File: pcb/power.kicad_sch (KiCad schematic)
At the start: 43 parts, among them Q1 AO3407A, Q2 PMV20EN, Q3 NCE3401AY, Q4 NCE3401AY, Q5 DMMT5401, U2 AP63200T

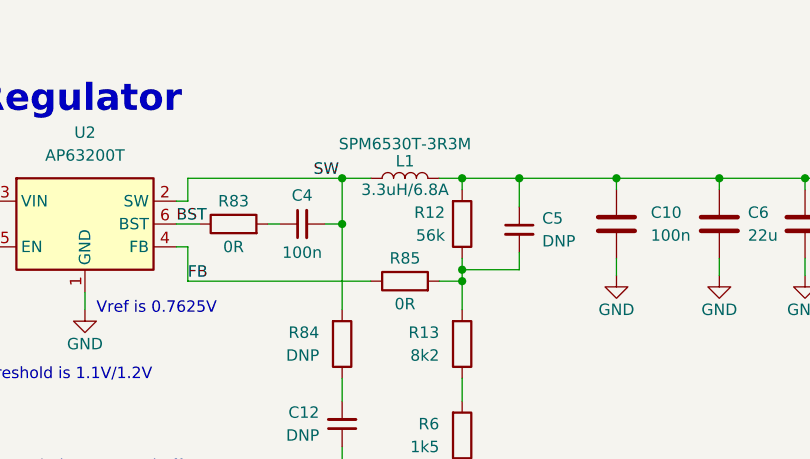
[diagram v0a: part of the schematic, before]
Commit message: Update to kicad 8
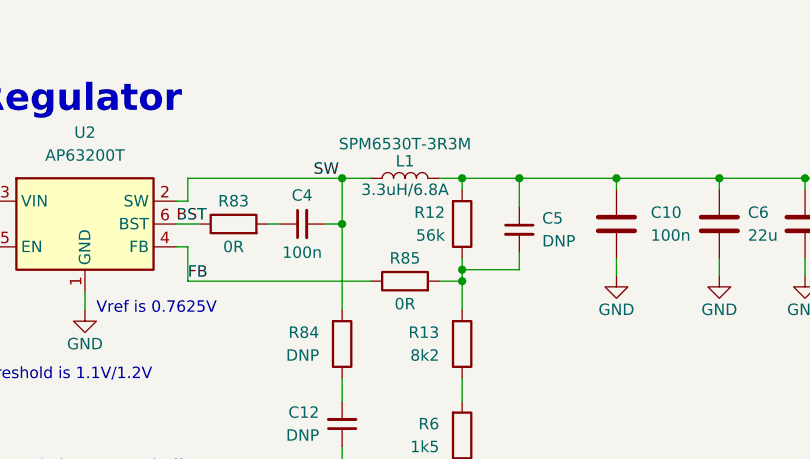
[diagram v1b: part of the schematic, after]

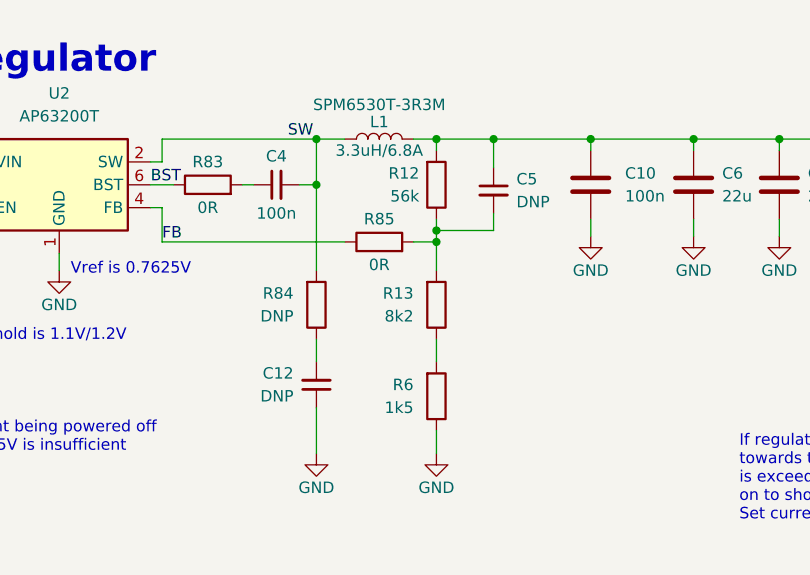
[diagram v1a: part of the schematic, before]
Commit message: Fix JLC part association
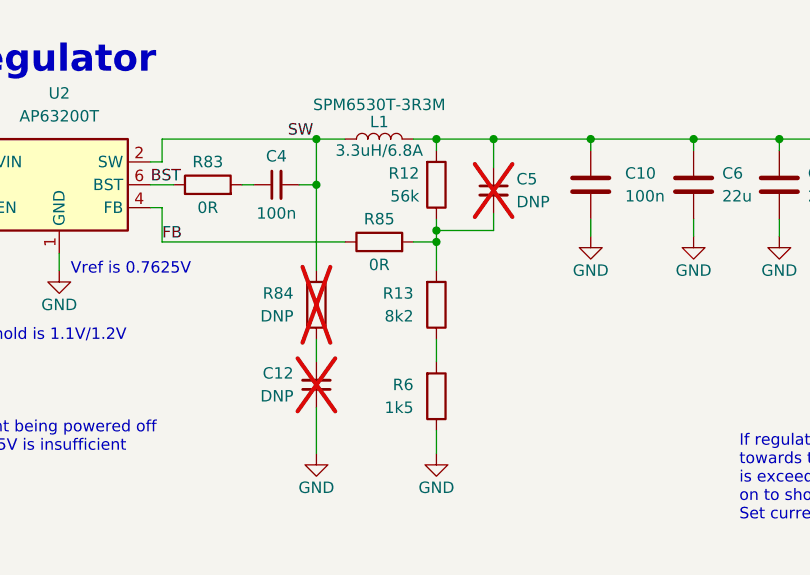
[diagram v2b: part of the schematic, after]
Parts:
- C10, C4, C9: JLC (none) -> C307331
- C11, C3, C6, C7, C8: JLC (none) -> C12891
- C12, C5, R84: now not fitted
- D2: JLC (none) -> C84256
- D3, D4, D5: JLC (none) -> C72043
- D6: JLC (none) -> C173404
- F1: JLC (none) -> C122965
- L1: JLC (none) -> C76856
- Q1: JLC (none) -> C15155
- Q2: JLC (none) -> C456088
- Q3, Q4: JLC (none) -> C169815
- Q5: JLC (none) -> C154733
- R10, R11: JLC (none) -> C25890
- R12: JLC (none) -> C25796
- R13: JLC (none) -> C25924
- R14: JLC (none) -> C25091
- R15, R4, R5, R7: JLC (none) -> C25744
- R16: JLC (none) -> C25792
- R6: JLC (none) -> C25867
- R8: JLC (none) -> C25741
- R83, R85: JLC (none) -> C17168
- R9: JLC (none) -> C25762

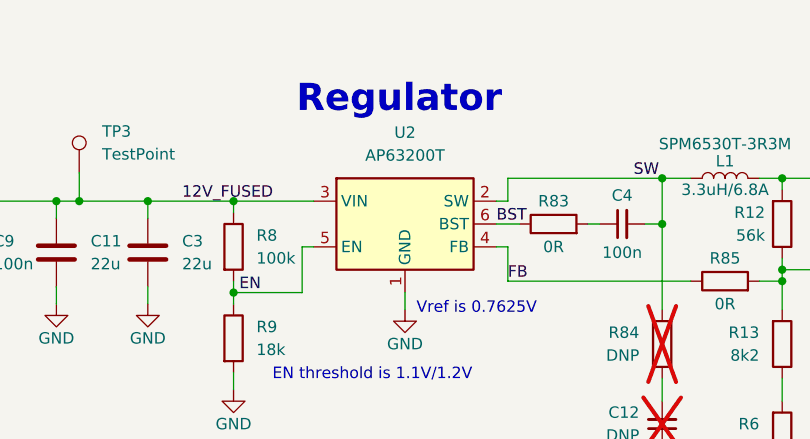
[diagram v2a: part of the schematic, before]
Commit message: Correct reg IC to AP62300T
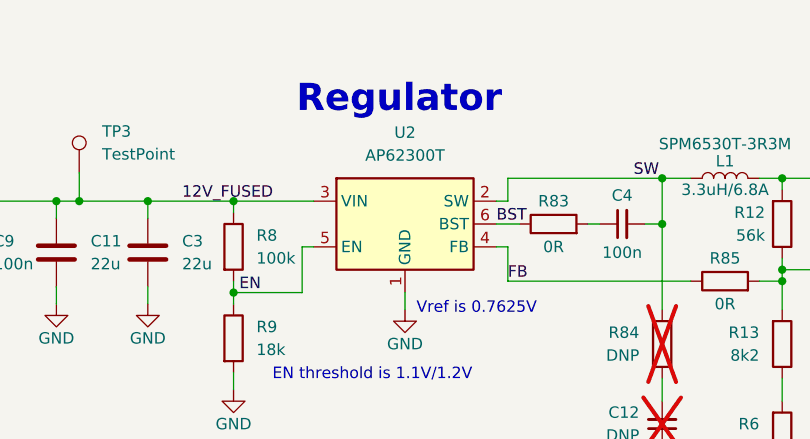
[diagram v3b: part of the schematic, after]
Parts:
- U2: value AP63200T -> AP62300T; JLC (none) -> C1883519
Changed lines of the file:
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@@
 			)
 		)
-		(property "Value" "AP63200T"
+		(property "Value" "AP62300T"
 			(at 111.76 58.42 0)
 			(effects
@@
 			)
 		)
-		(property "JLC" ""
+		(property "JLC" "C1883519"
 			(at 111.76 66.04 0)
 			(effects

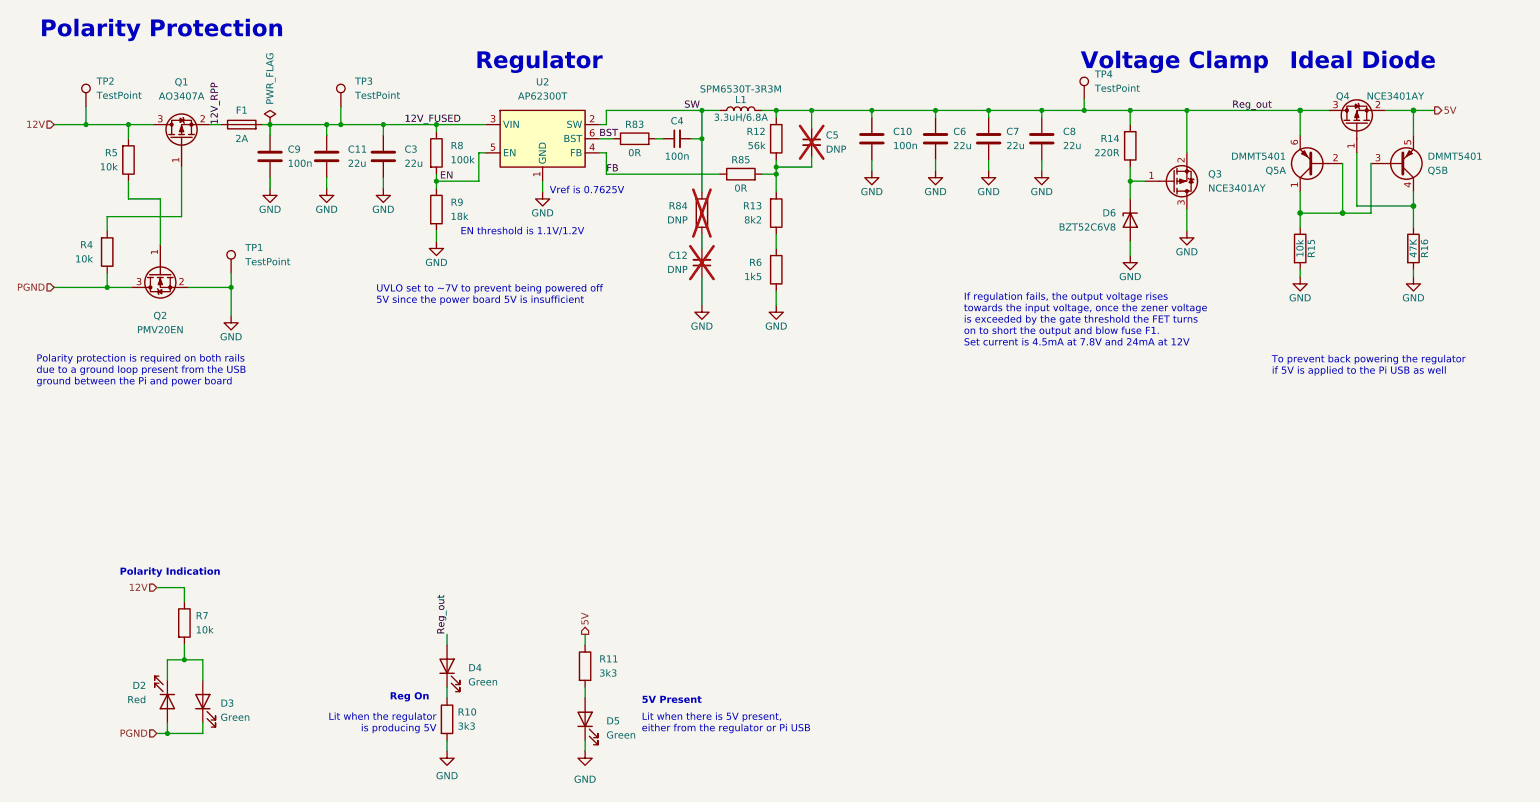
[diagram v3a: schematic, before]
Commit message: Fix ERC/DRC errors from Kicad 8
Mostly outdated library symbols and aligning the schmatic to the new grid
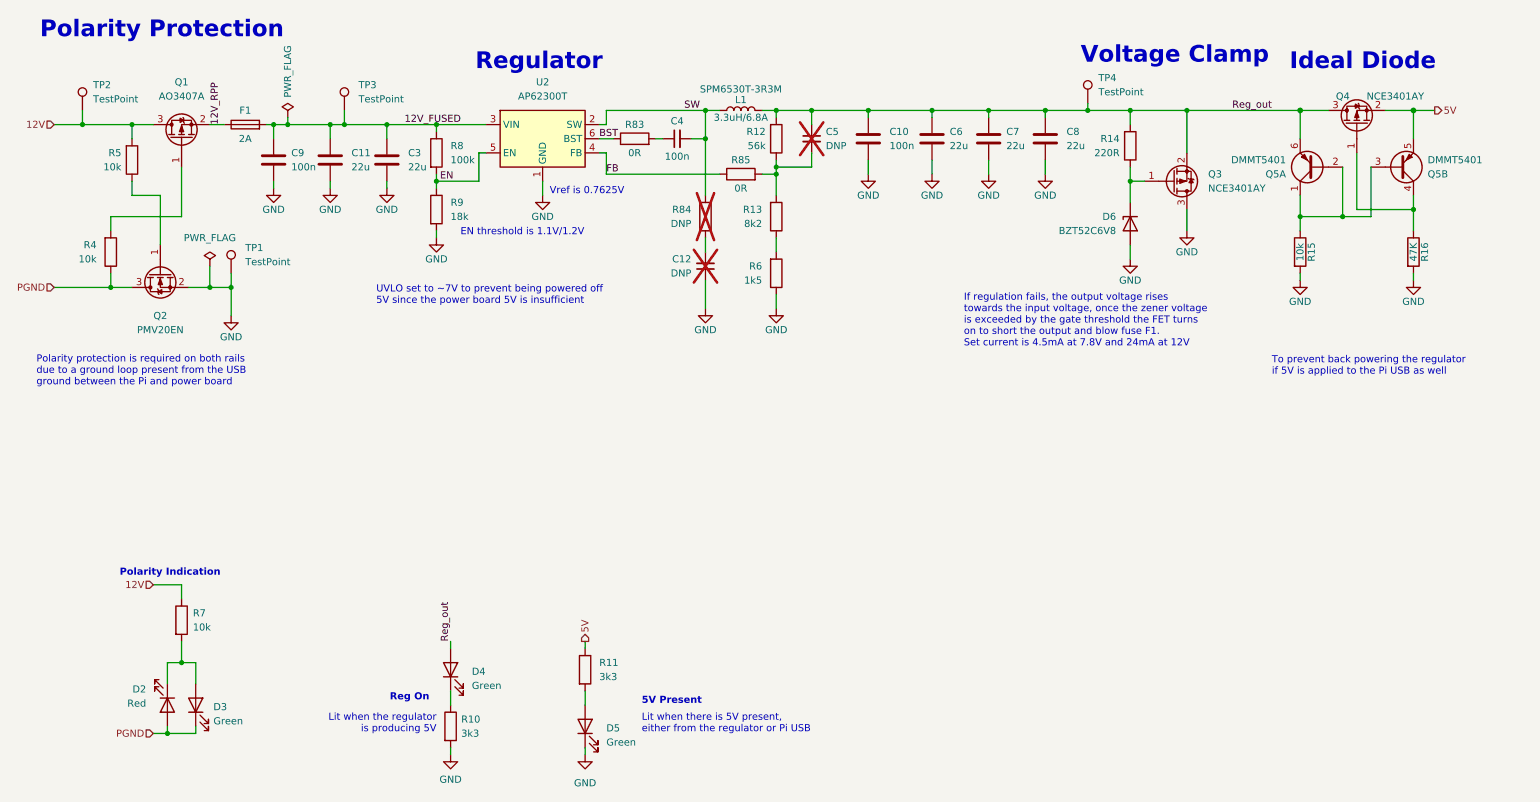
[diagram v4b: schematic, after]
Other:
- moved on the sheet: C10, C11, C12, C3, C5, C6, C8, C9, D2, D3, D4, D5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

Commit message: Update fuse to an equivalant with stock
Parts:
- F1: JLC C122965 -> C1972443
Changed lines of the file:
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@@
 			)
 		)
-		(property "Datasheet" "~"
+		(property "Datasheet" "https://wmsc.lcsc.com/wmsc/upload/file/pdf/v2/lcsc/2304140030_BOURNS-SF-0603S200-2_C1972443.pdf"
 			(at 58.42 63.5 0)
 			(effects
@@
 			)
 		)
-		(property "JLC" "C122965"
+		(property "JLC" "C1972443"
 			(at 58.42 63.5 0)
 			(effects

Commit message: Add U2 to pos file and correct rotation
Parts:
- U2: JLCPCB Rotation Offset (none) -> 90
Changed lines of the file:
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@@
+			)
+		)
+		(property "JLCPCB Rotation Offset" "90"
+			(at 111.76 66.04 0)
+			(effects
+				(font
+					(size 1.27 1.27)
+				)
+				(hide yes)
 			)
 		)
